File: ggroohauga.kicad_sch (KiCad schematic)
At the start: 7 parts

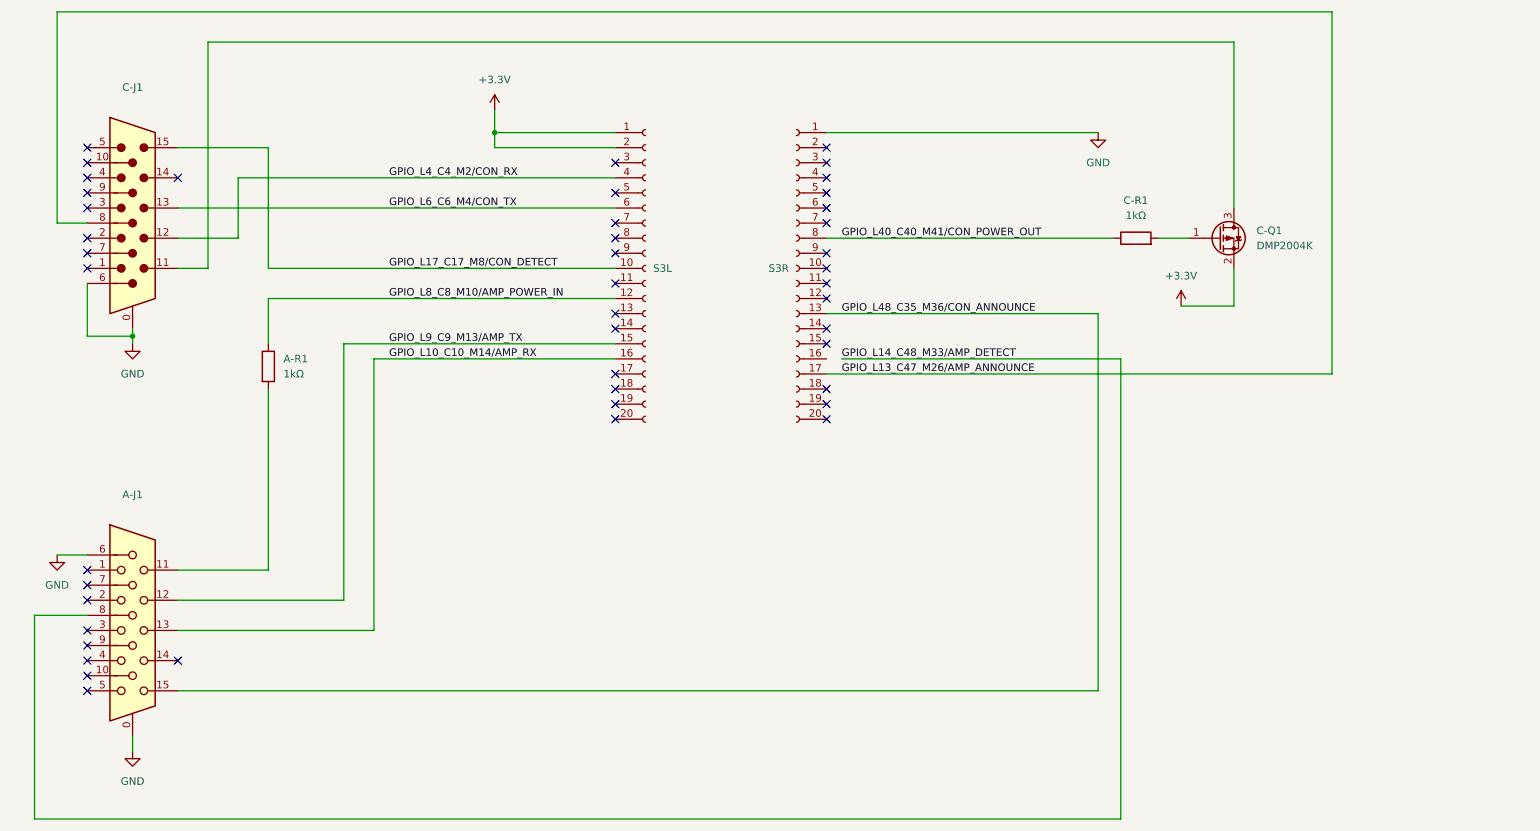
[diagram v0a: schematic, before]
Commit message: Create amplifier PCB
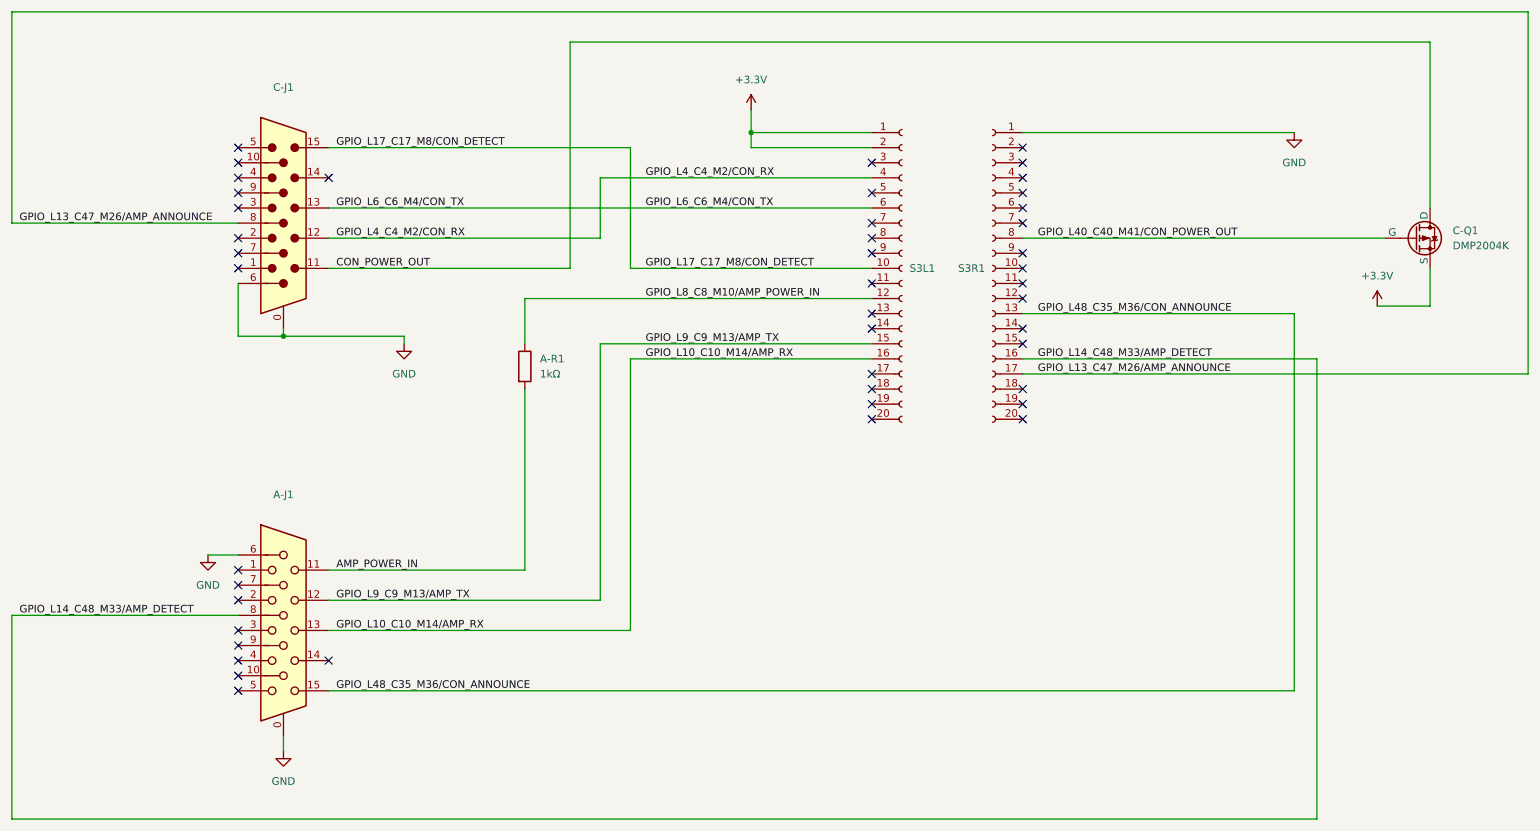
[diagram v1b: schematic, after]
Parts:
- removed C-Q1: DMP2004K, Package_TO_SOT_SMD:SOT-23, symbol Transistor_FET:DMG2301L
- removed C-R1: 1kΩ, symbol Device:R
- added C-Q1: DMP2004K, Package_TO_SOT_SMD:SOT-23, symbol Simulation_SPICE:PMOS
- A-J1: footprint (none) -> Amphenol:AMPHENOL_L77HDE15SD1CH4R
- A-R1: footprint (none) -> Resistor_SMD:R_0805_2012Metric_Pad1.20x1.40mm_HandSolder
- C-J1: footprint (none) -> Amphenol:AMPHENOL_L717HDE15PD1CH4F
- S3L1: renamed from S3L; footprint (none) -> Connector_PinSocket_2.54mm:PinSocket_1x20_P2.54mm_Vertical
- S3R1: renamed from S3R; footprint (none) -> Connector_PinSocket_2.54mm:PinSocket_1x20_P2.54mm_Vertical
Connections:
- net +3.3V: now also C-Q1.3 (S)
- net GPIO_L14_C48_M33/AMP_DETECT: now also S3R1.16 (Pin_16)
- net GPIO_L40_C40_M41/CON_POWER_OUT: now also C-Q1.2 (G)
- net AMP_POWER_IN: now reaches A-J1.11, A-R1.2
- net CON_POWER_OUT: now reaches C-J1.11
- net CON_POWER_OUT: now also C-Q1.1 (D)
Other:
- moved on the sheet: A-J1, A-R1, C-J1, S3L1, S3R1
